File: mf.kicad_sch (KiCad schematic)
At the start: 0 parts

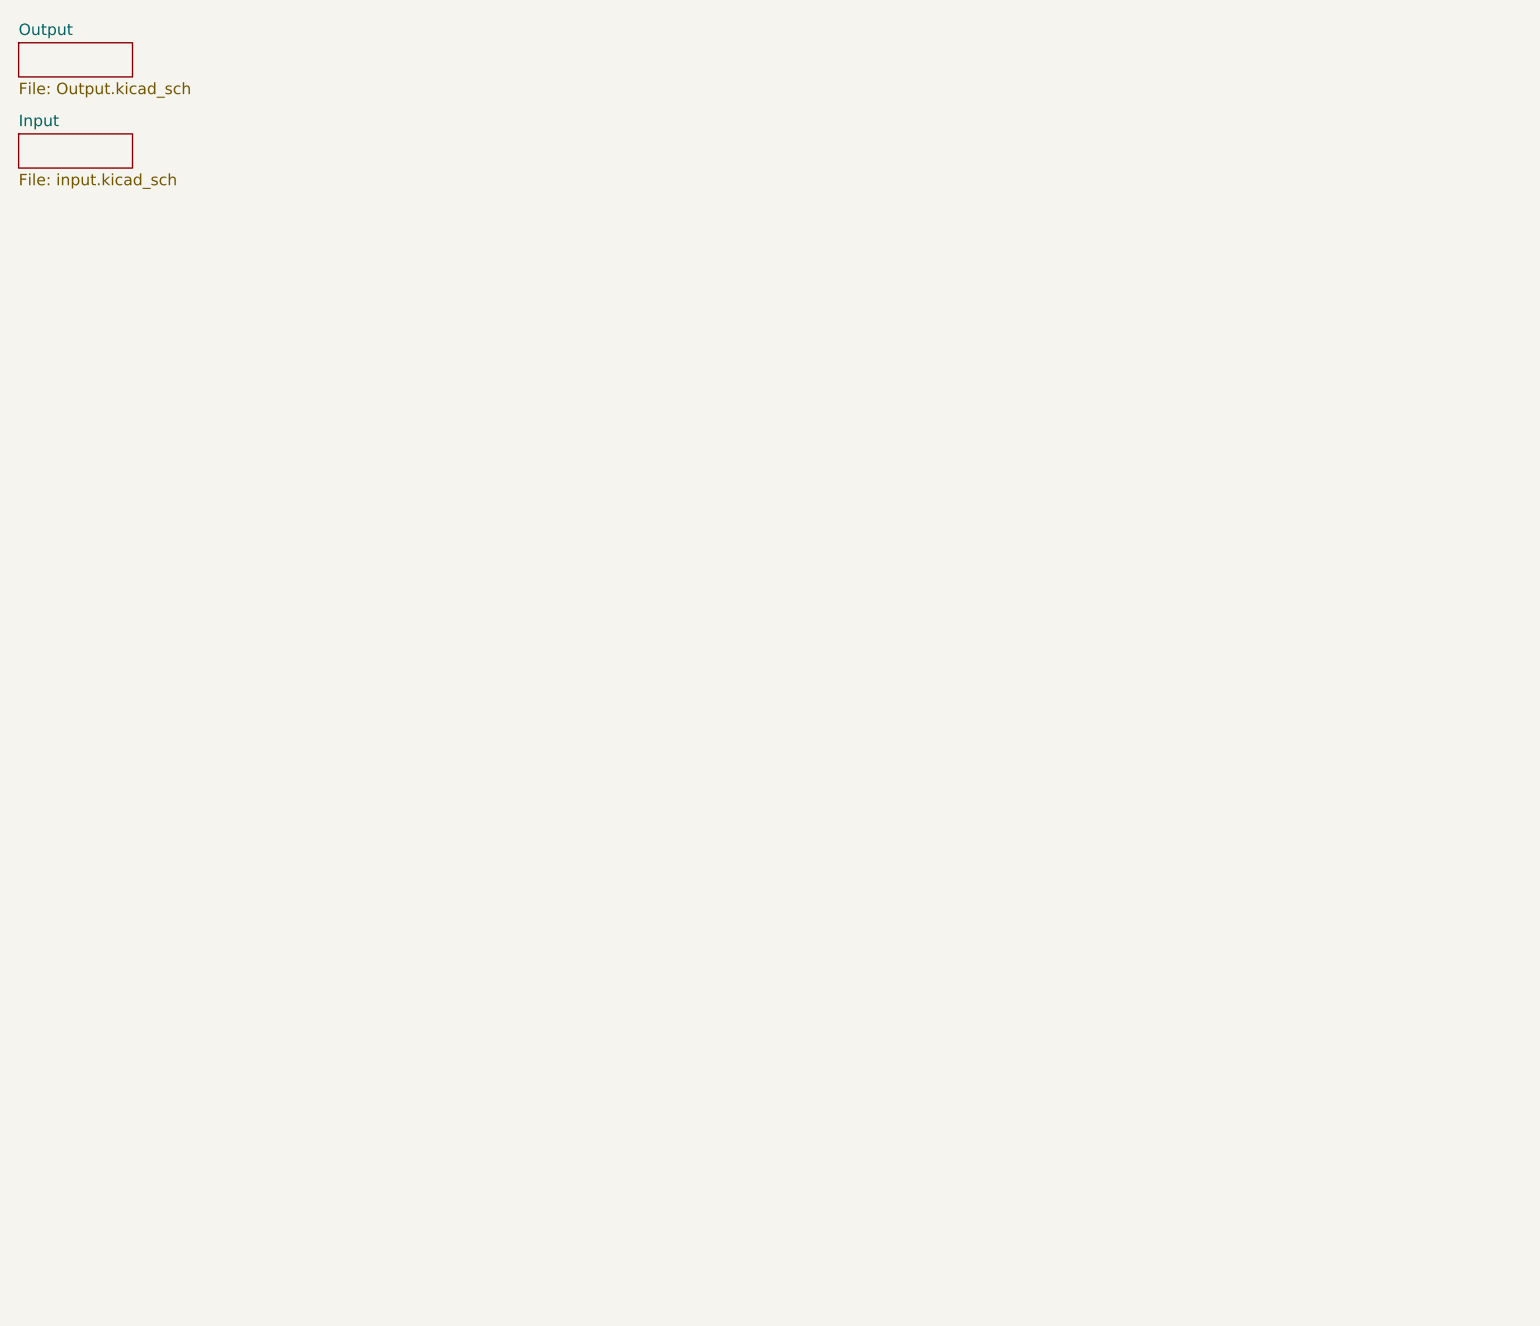
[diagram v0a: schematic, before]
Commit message: New schematic
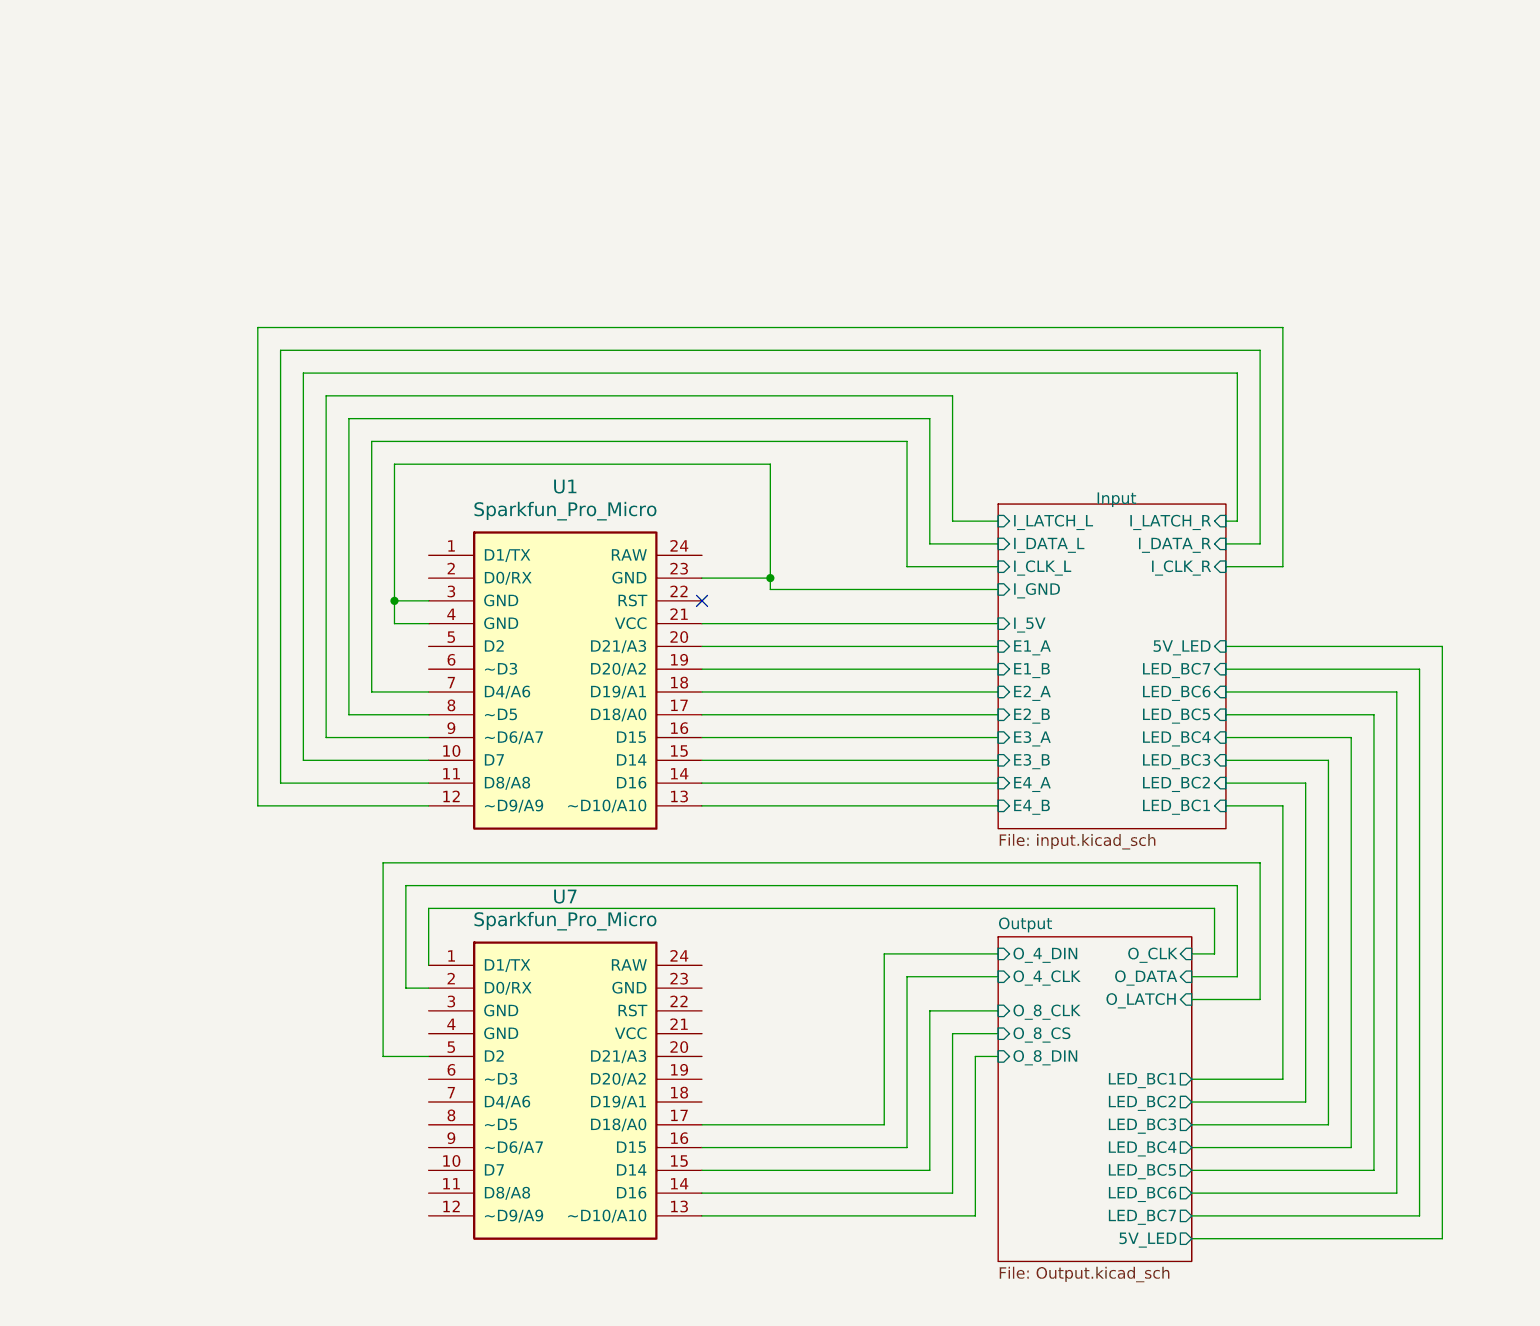
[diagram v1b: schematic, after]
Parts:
- added U1, U7: Sparkfun_Pro_Micro, Arduino:Sparkfun_Pro_Micro, symbol Promicro:Sparkfun_Pro_Micro
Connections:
- new net Input/E1_A: U1.20 (D21/A3)
- new net Input/E1_B: U1.19 (D20/A2)
- new net Input/E2_A: U1.18 (D19/A1)
- new net Input/E2_B: U1.17 (D18/A0)
- new net Input/E3_A: U1.16 (D15)
- new net Input/E3_B: U1.15 (D14)
- new net Input/E4_A: U1.14 (D16)
- new net Input/E4_B: U1.13 (~D10/A10)
- new net Input/I_5V: U1.21 (VCC)
- new net Input/I_CLK_L: U1.7 (D4/A6)
- new net Input/I_CLK_R: U1.12 (~D9/A9)
- new net Input/I_DATA_L: U1.8 (~D5)
- new net Input/I_DATA_R: U1.11 (D8/A8)
- new net Input/I_GND: U1.23 (GND), U1.3 (GND), U1.4 (GND)
- new net Input/I_LATCH_L: U1.9 (~D6/A7)
- new net Input/I_LATCH_R: U1.10 (D7)
- new net Output/O_4_CLK: U7.16 (D15)
- new net Output/O_4_DIN: U7.17 (D18/A0)
- new net Output/O_8_CLK: U7.15 (D14)
- new net Output/O_8_CS: U7.14 (D16)
- new net Output/O_8_DIN: U7.13 (~D10/A10)
- new net Output/O_CLK: U7.1 (D1/TX)
- new net Output/O_DATA: U7.2 (D0/RX)
- new net Output/O_LATCH: U7.5 (D2)
- no-connect marks 0 -> 1
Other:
- sheet Input ports: added 5V_LED, E1_A, E1_B, E2_A, E2_B, E3_A, E3_B, E4_A, E4_B, I_5V, I_CLK_L, I_CLK_R, I_DATA_L, I_DATA_R, I_GND, I_LATCH_L, I_LATCH_R, LED_BC1, LED_BC2, LED_BC3, LED_BC4, LED_BC5, LED_BC6, LED_BC7; removed none
- sheet Output ports: added 5V_LED, LED_BC1, LED_BC2, LED_BC3, LED_BC4, LED_BC5, LED_BC6, LED_BC7, O_4_CLK, O_4_DIN, O_8_CLK, O_8_CS, O_8_DIN, O_CLK, O_DATA, O_LATCH; removed none

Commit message: Update schematic with nearly everything
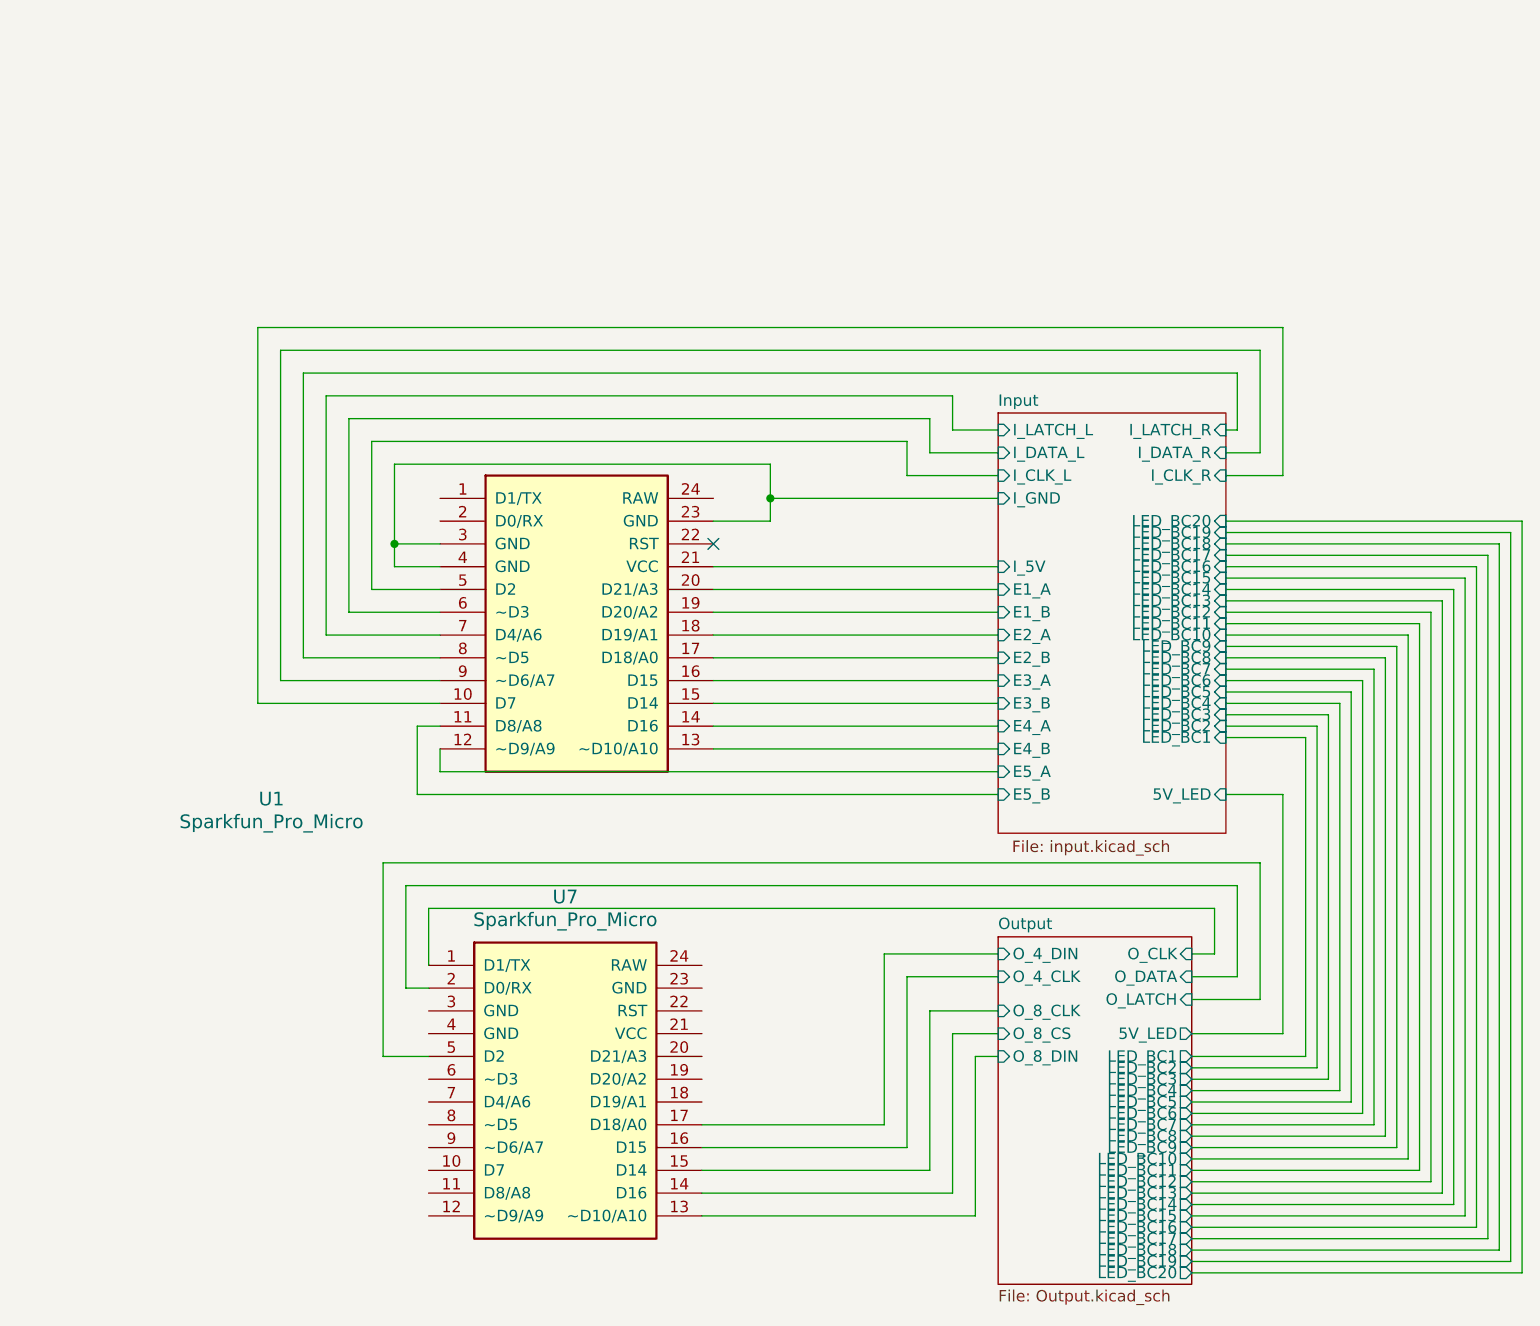
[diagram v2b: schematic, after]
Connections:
- net Input/I_CLK_L: now also U1.5 (D2); no longer U1.7 (D4/A6)
- net Input/I_CLK_R: now also U1.10 (D7); no longer U1.12 (~D9/A9)
- net Input/I_DATA_L: now also U1.6 (~D3); no longer U1.8 (~D5)
- net Input/I_DATA_R: now also U1.9 (~D6/A7); no longer U1.11 (D8/A8)
- net Input/I_LATCH_L: now also U1.7 (D4/A6); no longer U1.9 (~D6/A7)
- net Input/I_LATCH_R: now also U1.8 (~D5); no longer U1.10 (D7)
- new net Input/E5_A: U1.12 (~D9/A9)
- new net Input/E5_B: U1.11 (D8/A8)
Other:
- sheet Input ports: added E5_A, E5_B, LED_BC10, LED_BC11, LED_BC12, LED_BC13, LED_BC14, LED_BC15, LED_BC16, LED_BC17, LED_BC18, LED_BC19, LED_BC20, LED_BC8, LED_BC9; removed none
- sheet Output ports: added LED_BC10, LED_BC11, LED_BC12, LED_BC13, LED_BC14, LED_BC15, LED_BC16, LED_BC17, LED_BC18, LED_BC19, LED_BC20, LED_BC8, LED_BC9; removed none
- moved on the sheet: U1

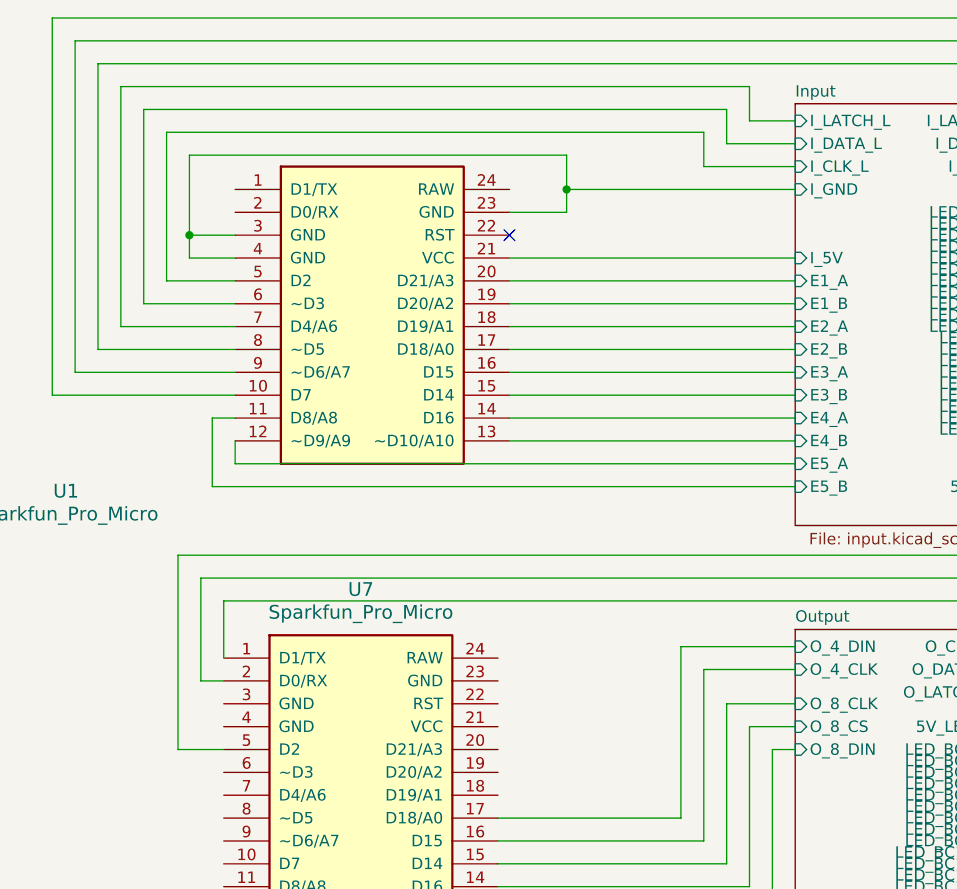
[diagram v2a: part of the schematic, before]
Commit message: Begin PCB routing + change in schematic
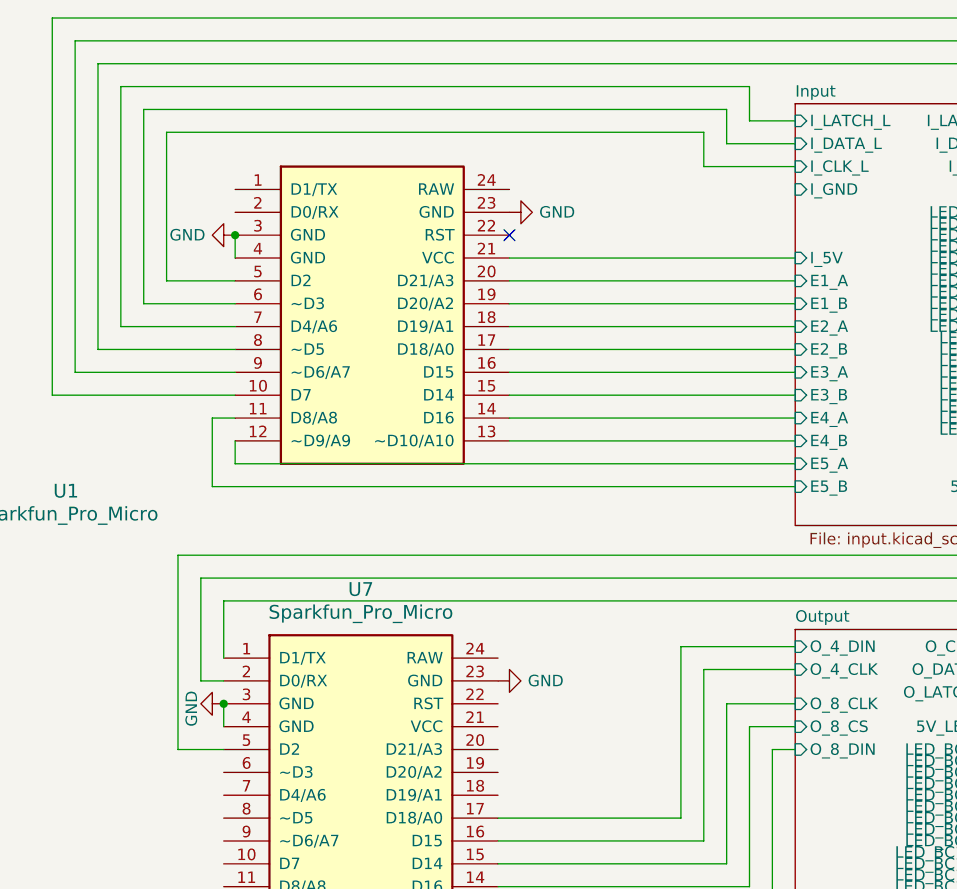
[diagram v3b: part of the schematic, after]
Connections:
- net Input/I_GND: no longer U1.23 (GND), U1.3 (GND), U1.4 (GND)
- net GND: now reaches U7.23 (GND)
- net GND: now also U1.23 (GND), U1.3 (GND), U1.4 (GND), U7.3 (GND), U7.4 (GND)
